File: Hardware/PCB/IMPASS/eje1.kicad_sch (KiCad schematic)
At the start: 8 parts, among them Q10 DMN3008SFG, Q11 DMN3008SFG, Q12 DMN3008SFG, Q13 DMN3008SFG, Q14 DMN3008SFG, Q15 DMN3008SFG, Q16 DMN3008SFG, Q9 DMN3008SFG

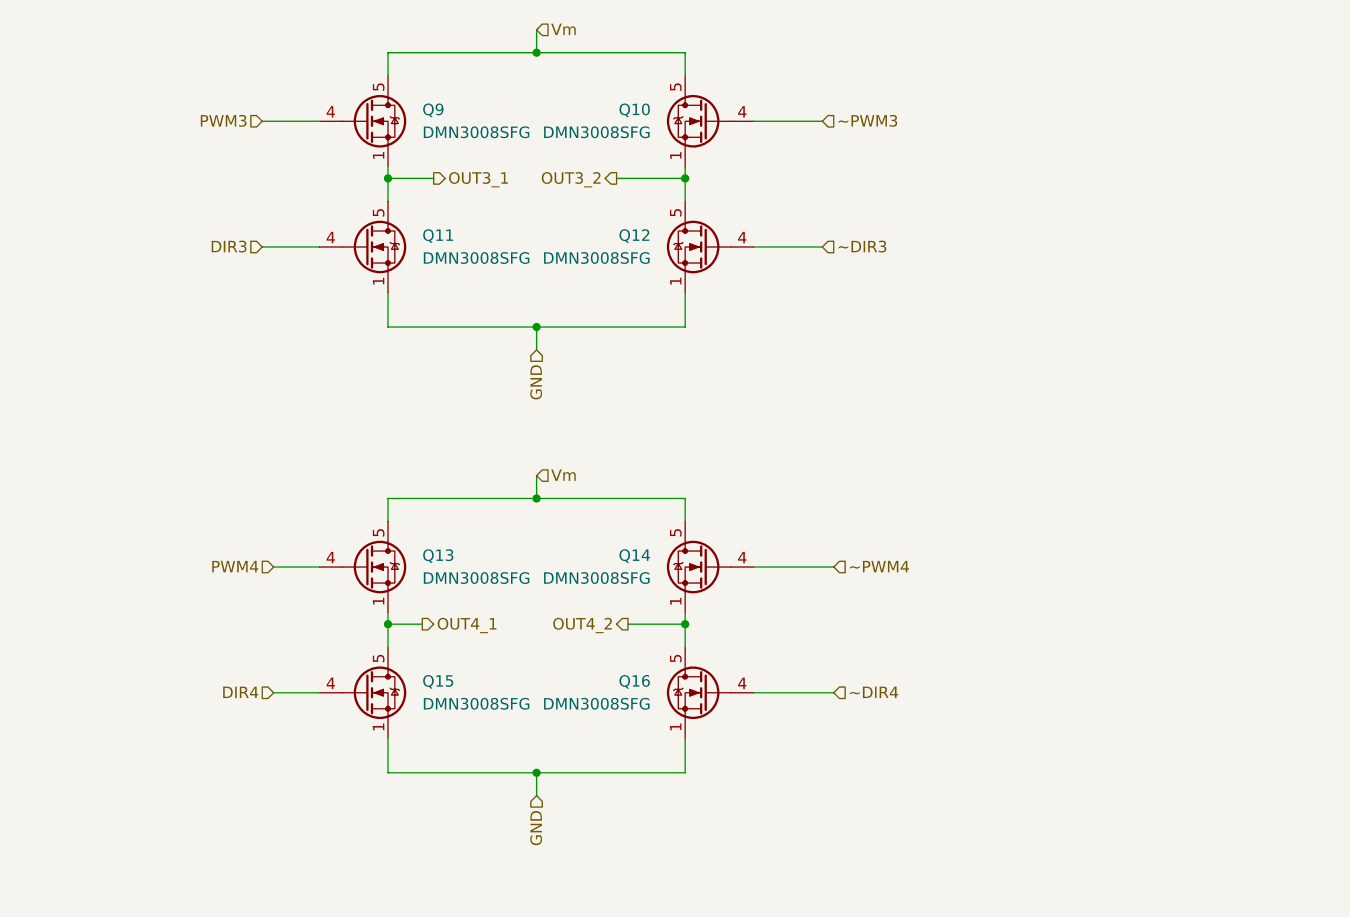
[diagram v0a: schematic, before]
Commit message: Restore all the schematics
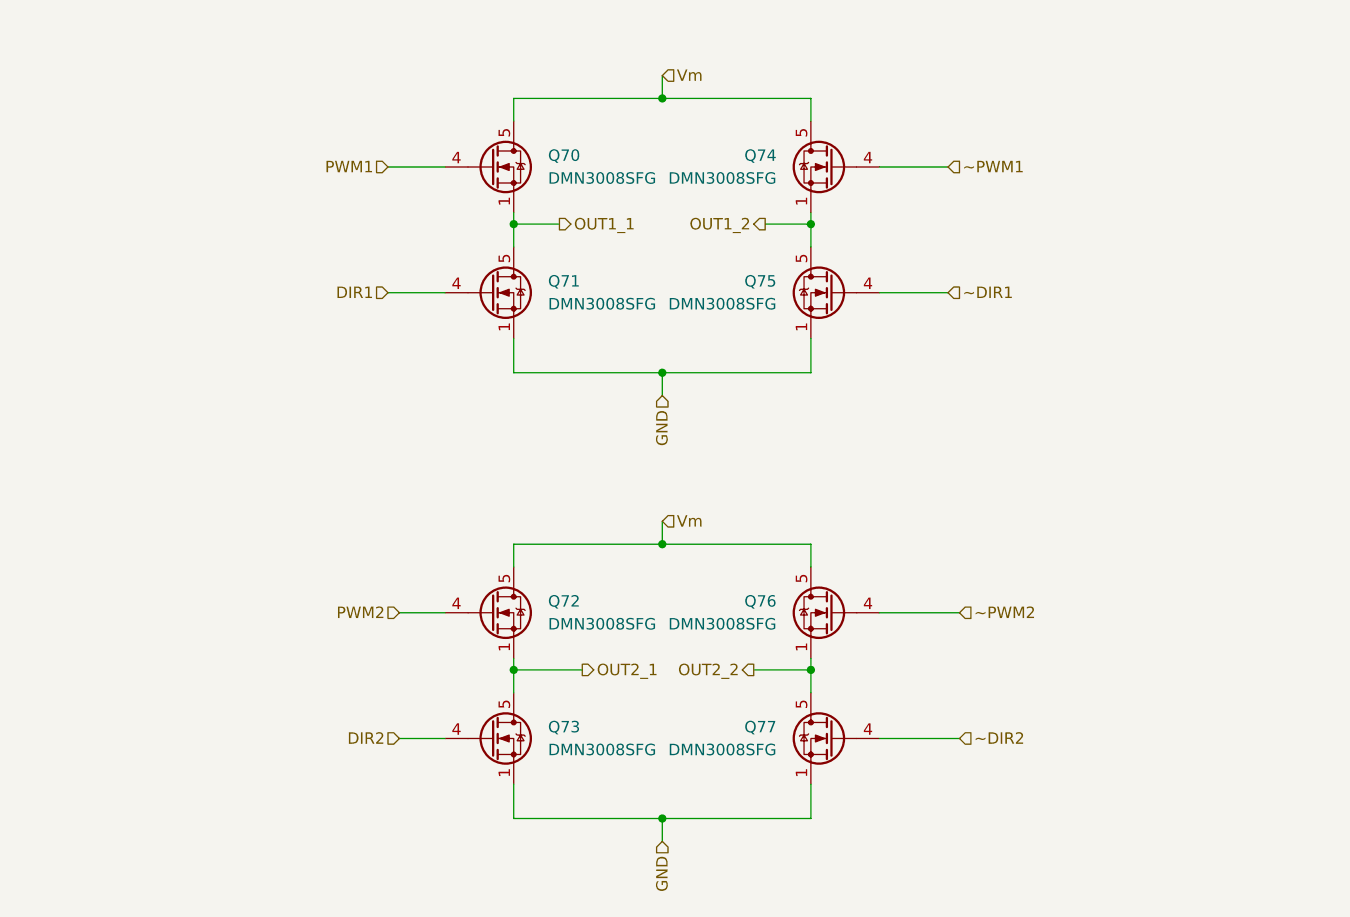
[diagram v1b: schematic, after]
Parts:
- removed Q10, Q11, Q12, Q13, Q14, Q15, Q16, Q9: DMN3008SFG, Package_SON:Diodes_PowerDI3333-8, symbol Transistor_FET:DMN3008SFG
- added Q70, Q71, Q72, Q73, Q74, Q75, Q76, Q77: DMN3008SFG, Package_SON:Diodes_PowerDI3333-8, symbol Transistor_FET:DMN3008SFG
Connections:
- net GND: now also Q71.1 (S), Q71.2 (S), Q71.3 (S), Q73.1 (S), Q73.2 (S), Q73.3 (S), Q75.1 (S), Q75.2 (S), Q75.3 (S), Q77.1 (S), Q77.2 (S), Q77.3 (S)
- net Vm: now also Q70.5 (D), Q72.5 (D), Q74.5 (D), Q76.5 (D)
- new net DIR1: Q71.4 (G)
- new net DIR2: Q73.4 (G)
- new net OUT1_1: Q70.1 (S), Q70.2 (S), Q70.3 (S), Q71.5 (D)
- new net OUT1_2: Q74.1 (S), Q74.2 (S), Q74.3 (S), Q75.5 (D)
- new net OUT2_1: Q72.1 (S), Q72.2 (S), Q72.3 (S), Q73.5 (D)
- new net OUT2_2: Q76.1 (S), Q76.2 (S), Q76.3 (S), Q77.5 (D)
- new net PWM1: Q70.4 (G)
- new net PWM2: Q72.4 (G)
- new net ~DIR1: Q75.4 (G)
- new net ~DIR2: Q77.4 (G)
- new net ~PWM1: Q74.4 (G)
- new net ~PWM2: Q76.4 (G)

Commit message: Hardware: update schematic and PCB layout
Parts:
- removed Q70, Q72, Q74, Q76: DMN3008SFG, Package_SON:Diodes_PowerDI3333-8, symbol Transistor_FET:DMN3008SFG
- added Q1, Q5: BC847BDW1, Package_TO_SOT_SMD:SOT-363_SC-70-6, symbol Transistor_BJT:BC847BDW1
- added Q2, Q3, Q4, Q6: DMP3013SFV, Package_SON:Diodes_PowerDI3333-8, symbol Transistor_FET:DMP3013SFV
- added R59, R60, R61, R62, R63, R64, R65, R66: 10k, Resistor_SMD:R_0603_1608Metric, symbol Device:R
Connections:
- net GND: now also Q1.1 (E1), Q1.4 (E2), Q5.1 (E1), Q5.4 (E2)
- net OUT1_1: now also Q2.5 (D)
- net OUT1_2: now also Q3.5 (D)
- net OUT2_1: now also Q4.5 (D)
- net OUT2_2: now also Q6.5 (D)
- net PWM1: now also R61.1
- net PWM2: now also R63.1
- net Vm: now also Q2.1 (S), Q2.2 (S), Q2.3 (S), Q3.1 (S), Q3.2 (S), Q3.3 (S), Q4.1 (S), Q4.2 (S), Q4.3 (S), Q6.1 (S), Q6.2 (S), Q6.3 (S), R59.1, R60.1, R64.1, R65.1
- net ~PWM1: now also R62.2
- net ~PWM2: now also R66.2
- new net: Q5.5 (B2), R66.1
- new net: Q1.3 (C2), Q3.4 (G), R60.2
- new net: Q1.5 (B2), R62.1
- new net: Q5.3 (C2), Q6.4 (G), R65.2
- new net: Q4.4 (G), Q5.6 (C1), R64.2
- new net: Q1.2 (B1), R61.2
- new net: Q1.6 (C1), Q2.4 (G), R59.2
- new net: Q5.2 (B1), R63.2
